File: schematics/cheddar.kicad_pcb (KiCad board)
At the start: 2 copper layers, 43 x 26 mm, 30 parts, among them J1 USB_OTG, J3 Conn_01x08, J5 BATT_CONN, Q1 MOSFET_PCH, U1 CH340G, U2 MCP73831, U4 HT7333, Y1 12Mhz

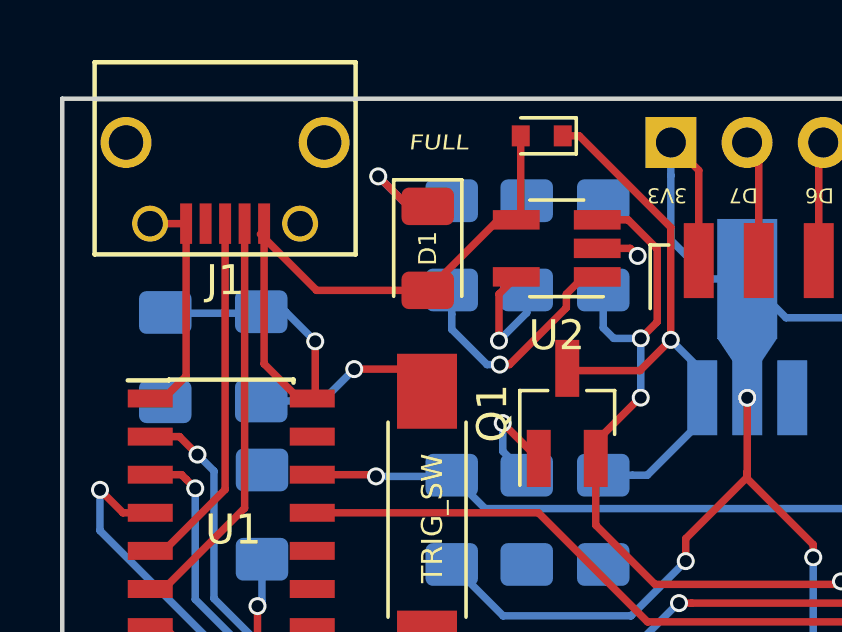
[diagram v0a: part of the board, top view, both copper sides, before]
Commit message: Remove useless labeling
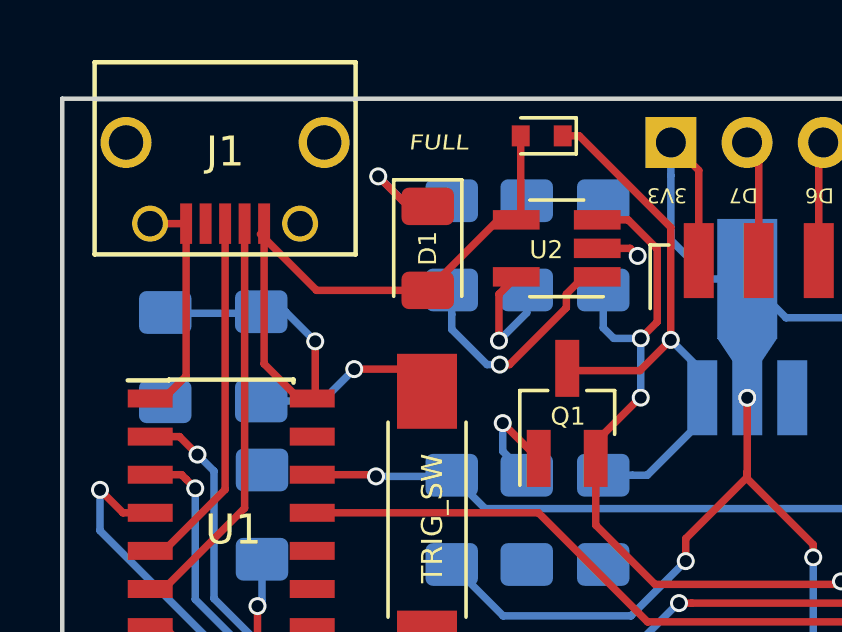
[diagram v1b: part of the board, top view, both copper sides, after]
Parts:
- renumbered J3 to ?, J5 to BAT_CONN
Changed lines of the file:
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@@
     (tags "USB USB_B USB_micro USB_OTG")
     (attr smd)
-    (fp_text reference J1 (at 0 -3.45 180) (layer F.SilkS)
+    (fp_text reference J1 (at 0 0.839 180) (layer F.SilkS)
       (effects (font (size 1 1) (thickness 0.15)))
     )
@@
     (descr "Through hole straight pin header, 1x08, 2.54mm pitch, single row")
     (tags "Through hole pin header THT 1x08 2.54mm single row")
-    (fp_text reference J3 (at 0 2.33 90) (layer B.SilkS)
+    (fp_text reference "" (at 0 2.33 90) (layer B.SilkS)
       (effects (font (size 1 1) (thickness 0.15)) (justify mirror))
     )
@@
     (tags "SOT-23-5 hand-soldering")
     (attr smd)
-    (fp_text reference U2 (at 0 -2.9 180) (layer F.SilkS)
-      (effects (font (size 1 1) (thickness 0.15)))
+    (fp_text reference U2 (at 0.35 -0.05 180) (layer F.SilkS)
+      (effects (font (size 0.6 0.6) (thickness 0.08)))
     )
     (fp_text value MCP73831 (at 0 2.9 180) (layer F.Fab)
@@
     (tags "resistor handsolder")
     (attr smd)
-    (fp_text reference J5 (at 0 1.82 270) (layer B.SilkS)
-      (effects (font (size 1 1) (thickness 0.15)) (justify mirror))
+    (fp_text reference BAT_CONN (at 0 1.82 270) (layer B.SilkS)
+      (effects (font (size 0.8 0.8) (thickness 0.1)) (justify mirror))
     )
     (fp_text value BATT_CONN (at 0 -1.82 270) (layer B.Fab)
@@
     (pad 2 smd roundrect (at 1.4875 0 270) (size 1.425 1.75) (layers B.Cu B.Paste B.Mask) (roundrect_rratio 0.175439)
       (net 20 "Net-(C7-Pad2)"))
-    (model ${KISYS3DMOD}/Resistor_SMD.3dshapes/R_1206_3216Metric.wrl
-      (at (xyz 0 0 0))
-      (scale (xyz 1 1 1))
-      (rotate (xyz 0 0 0))
-    )
   )
   (module Package_TO_SOT_SMD:SOT-23_Handsoldering (layer F.Cu)
@@
     (tags SOT-23)
     (attr smd)
-    (fp_text reference Q1 (at 0 -2.5 90) (layer F.SilkS)
-      (effects (font (size 1 1) (thickness 0.15)))
+    (fp_text reference Q1 (at -0.1 0.025 180) (layer F.SilkS)
+      (effects (font (size 0.6 0.6) (thickness 0.08)))
     )
     (fp_text value MOSFET_PCH (at 0 2.5 90) (layer F.Fab)

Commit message: [enh] better routing
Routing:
- net +5V: track 31.0 -> 13.9 mm
- net GND: track 30.9 -> 40.4 mm, vias 2 -> 4
- net +3V3: track 47.9 -> 55.1 mm, vias 3 -> 0
- net Net-(D1-Pad1): track 4.85 -> 0.88 mm
- net Net-(C3-Pad1): track 14.6 -> 11.2 mm
- net Net-(R1-Pad1): track 4.43 -> 1.42 mm
- net Net-(R3-Pad1): track 8.13 -> 6.16 mm
- net /GPIO16: track 52.3 -> 53.6 mm
